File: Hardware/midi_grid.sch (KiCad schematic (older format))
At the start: 10 parts, among them J1 USB_OTG, J2 3.5mm jack, J3 3.5mm jack, M1 Mounting_hole, M2 Mounting_hole, M3 Mounting_hole

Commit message: linked footprints with 3D models in project directory
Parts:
- J1: Catalog link (none) -> https://www.lemona.lt/?page=item&i_id=216110
- J2, J3: Catalog link (none) -> http://lt.farnell.com/cliff-electronic-components/fc68133/s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
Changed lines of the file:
@@
 F 2 "project_library:USB_Micro-B_Molex-105017-0001" H 1950 3950 50  0001 C CNN
 F 3 "" H 1950 3950 50  0001 C CNN
+F 4 "https://www.lemona.lt/?page=item&i_id=216110" H 1800 4000 60  0001 C CNN "Catalog link"
 	1    1800 4000
 	1    0    0    -1
@@
 F 2 "project_library:3.5mm-jack" H 2950 4600 50  0001 C CNN
 F 3 "" H 2950 4600 50  0001 C CNN
+F 4 "http://lt.farnell.com/cliff-electronic-components/fc68133/stereo-jack-3-5mm-5pos-pcb/dp/2518190" H 2700 4500 60  0001 C CNN "Catalog link"
 	1    2700 4500
 	1    0    0    -1
@@
 F 2 "project_library:3.5mm-jack" H 2950 5200 50  0001 C CNN
 F 3 "" H 2950 5200 50  0001 C CNN
+F 4 "http://lt.farnell.com/cliff-electronic-components/fc68133/stereo-jack-3-5mm-5pos-pcb/dp/2518190" H 2700 5100 60  0001 C CNN "Catalog link"
 	1    2700 5100
 	1    0    0    -1

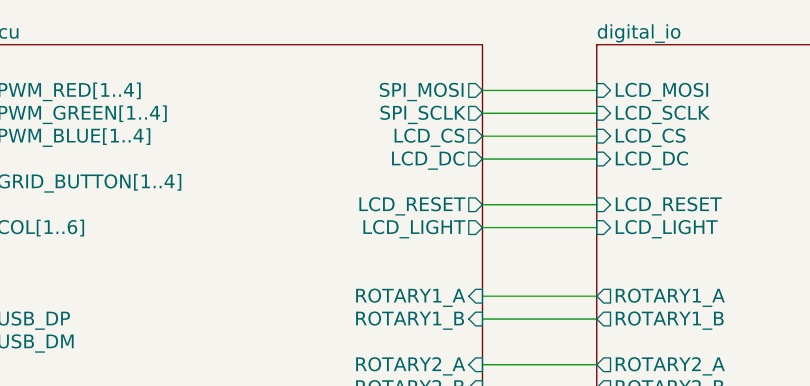
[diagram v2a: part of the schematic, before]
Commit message: rerouted LCD_LIGHT pin to PB5
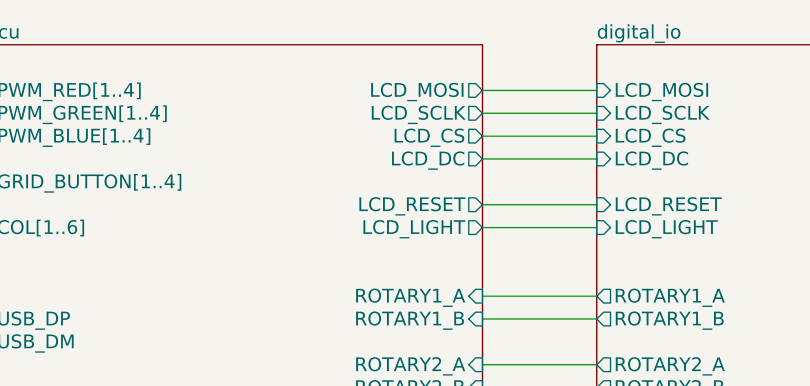
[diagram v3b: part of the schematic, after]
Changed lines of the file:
@@
 F12 "ROTARY2_A" I R 7500 4200 60
 F13 "ROTARY2_B" I R 7500 4300 60
-F14 "SPI_MOSI" O R 7500 3000 60
-F15 "SPI_SCLK" O R 7500 3100 60
+F14 "LCD_MOSI" O R 7500 3000 60
+F15 "LCD_SCLK" O R 7500 3100 60
 F16 "LCD_LIGHT" O R 7500 3600 60
 F17 "LCD_DC" O R 7500 3300 60

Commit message: converted all components except big tactile switches
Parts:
- GR1, GR2, GR3, GR4: symbol Graphical -> project_library:Graphical
- J1: symbol USB_OTG -> project_library:USB_OTG
- J2, J3: symbol Audio-Jack-3_2Switches -> project_library:Audio-Jack-3_2Switches
- M1, M2, M3: symbol Mounting_hole -> project_library:Mounting_hole
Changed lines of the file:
@@
-EESchema Schematic File Version 2
-LIBS:project_library
-LIBS:power
-LIBS:device
-LIBS:switches
-LIBS:relays
-LIBS:motors
-LIBS:transistors
-LIBS:conn
-LIBS:linear
-LIBS:regul
-LIBS:74xx
-LIBS:cmos4000
-LIBS:adc-dac
-LIBS:memory
-LIBS:xilinx
-LIBS:microcontrollers
-LIBS:diode
-LIBS:dsp
-LIBS:microchip
-LIBS:analog_switches
-LIBS:motorola
-LIBS:texas
-LIBS:intel
-LIBS:audio
-LIBS:interface
-LIBS:digital-audio
-LIBS:philips
-LIBS:display
-LIBS:cypress
-LIBS:siliconi
-LIBS:opto
-LIBS:atmel
-LIBS:contrib
-LIBS:valves
-LIBS:stm32
-LIBS:ESD_Protection
+EESchema Schematic File Version 4
 LIBS:midi_grid-cache
-EELAYER 25 0
+EELAYER 30 0
 EELAYER END
 $Descr A4 11693 8268
@@
 	2300 3300 2500 3300
 $Comp
-L GND #PWR01
+L project_library:GND #PWR01
 U 1 1 5A326E77
 P 1800 4600
@@
 $EndComp
 Wire Wire Line
-	1800 4400 1800 4600
+	1800 4400 1800 4500
 Wire Wire Line
 	1800 4500 1700 4500
@@
 	2500 5300 2500 5400
 $Comp
-L GND #PWR02
+L project_library:GND #PWR02
 U 1 1 5A337D47
 P 2500 5400
@@
 $EndComp
 $Comp
-L USB_OTG J1
+L project_library:USB_OTG J1
 U 1 1 5A33503F
 P 1800 4000
@@
 NoConn ~ 2100 4200
 $Comp
-L Audio-Jack-3_2Switches J2
+L project_library:Audio-Jack-3_2Switches J2
 U 1 1 5A3F863B
 P 2700 4500
@@
 $EndComp
 $Comp
-L Audio-Jack-3_2Switches J3
+L project_library:Audio-Jack-3_2Switches J3
 U 1 1 5A422E89
 P 2700 5100
@@
 NoConn ~ 2900 4300
 $Comp
-L Graphical GR1
+L project_library:Graphical GR1
 U 1 1 5A53D346
 P 700 7100
@@
 $EndComp
 $Comp
-L Graphical GR2
+L project_library:Graphical GR2
 U 1 1 5A53DA73
 P 1100 7100
@@
 $EndComp
 $Comp
-L Graphical GR3
+L project_library:Graphical GR3
 U 1 1 5A6786D2
 P 1100 7500
@@
 $EndComp
 $Comp
-L Mounting_hole M1
+L project_library:Mounting_hole M1
 U 1 1 5A73E20A
 P 1500 7100
@@
 $EndComp
 $Comp
-L Mounting_hole M2
+L project_library:Mounting_hole M2
 U 1 1 5A740E09
 P 1900 7100
@@
 $EndComp
 $Comp
-L Mounting_hole M3
+L project_library:Mounting_hole M3
 U 1 1 5A740F4F
 P 1500 7500
@@
 $EndComp
 $Comp
-L Graphical GR4
+L project_library:Graphical GR4
 U 1 1 5A5BCF08
 P 700 7500
@@
 	1    0    0    -1
 $EndComp
+Wire Wire Line
+	1800 4500 1800 4600
 $EndSCHEMATC
